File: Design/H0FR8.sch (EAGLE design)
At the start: 43 parts, among them Q1 MMBT3904LT1, U1 STM32G0B1CEU6QFN_B1CEU6_STM-L, U2 T2035H-6GD2PAK_T2550_STM-M, U3 VOT8121AM-VT, U4 TLP184_GR-TPL,SE, U5 V275LA4P, X1 XTALL_CSTCE8M00G52

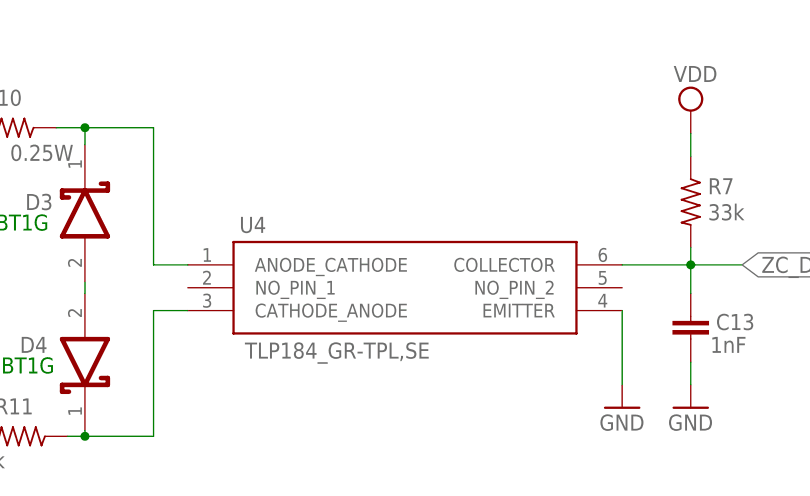
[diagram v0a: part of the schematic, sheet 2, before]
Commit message: - Fixed component's footprints and 3d packages.
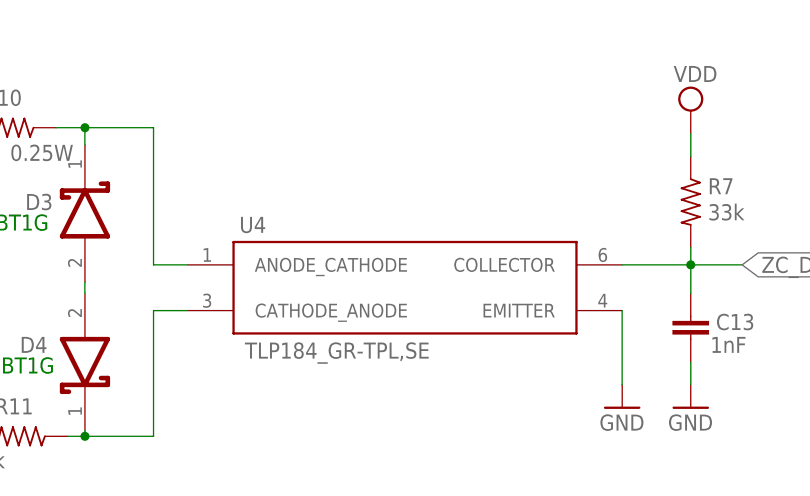
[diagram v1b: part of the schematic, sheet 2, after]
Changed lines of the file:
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@@
 <part name="FB1" library="HEXABITZ_RCLS" library_urn="urn:adsk.eagle:library:20064561" deviceset="FB-0603" device="" package3d_urn="urn:adsk.eagle:package:19666458/5"/>
 <part name="SUPPLY10" library="supply2" library_urn="urn:adsk.eagle:library:372" deviceset="VDD" device=""/>
-<part name="SWD" library="pinhead" deviceset="PINHD-1X3" device="" package3d_urn="urn:adsk.eagle:package:22458/2"/>
+<part name="SWD" library="pinhead" library_urn="urn:adsk.eagle:library:325" deviceset="PINHD-1X3" device="" package3d_urn="urn:adsk.eagle:package:22458/2"/>
 <part name="U1" library="HEXABITZ_ICs" library_urn="urn:adsk.eagle:library:20064554" deviceset="STM32G0B1CEU6" device="QFN_B1CEU6_STM-L" package3d_urn="urn:adsk.eagle:package:33547754/8"/>
 <part name="TRIMBLE-LOGO1" library="HEXABITZ_USER_INTERFACE_PARTS" library_urn="urn:adsk.eagle:library:20064563" deviceset="HEXA-LOGO-SCH" device=""/>
-<part name="TRIMBLE-LOGO2" library="HEXABITZ_USER_INTERFACE_PARTS" library_urn="urn:adsk.eagle:library:20064563" deviceset="HEXA-LOGO" device="" package3d_urn="urn:adsk.eagle:package:43807249/2"/>
+<part name="TRIMBLE-LOGO2" library="HEXABITZ_USER_INTERFACE_PARTS" library_urn="urn:adsk.eagle:library:20064563" deviceset="HEXA-LOGO" device="" package3d_urn="urn:adsk.eagle:package:43807249/3"/>
 <part name="D2" library="HEXABITZ_RCLS" library_urn="urn:adsk.eagle:library:20064561" deviceset="BOURNS_CDSOD323-T03SC" device="BOURNS_CDSOD323-T03SC_0_0" package3d_urn="urn:adsk.eagle:package:20526306/2"/>
 <part name="C10" library="HEXABITZ_RCLS" library_urn="urn:adsk.eagle:library:20064561" deviceset="C-0805" device="" package3d_urn="urn:adsk.eagle:package:19666489/4" value="10nF">
@@
 <part name="R4" library="HEXABITZ_RCLS" library_urn="urn:adsk.eagle:library:20064561" deviceset="R-0603" device="" package3d_urn="urn:adsk.eagle:package:1435818/6" value="1k"/>
 <part name="U2" library="HEXABITZ_ICs" library_urn="urn:adsk.eagle:library:20064554" deviceset="T2035H-6G" device="D2PAK_T2550_STM-M" package3d_urn="urn:adsk.eagle:package:44160048/2"/>
-<part name="U4" library="HEXABITZ_ICs" library_urn="urn:adsk.eagle:library:20064554" deviceset="TLP184_GR-TPL,SE" device="" package3d_urn="urn:adsk.eagle:package:44160045/2"/>
+<part name="U4" library="HEXABITZ_ICs" library_urn="urn:adsk.eagle:library:20064554" deviceset="TLP184_GR-TPL,SE" device="" package3d_urn="urn:adsk.eagle:package:45805681/2"/>
 <part name="U3" library="HEXABITZ_ICs" library_urn="urn:adsk.eagle:library:20064554" deviceset="VOT8121AM-VT" device="" package3d_urn="urn:adsk.eagle:package:44160046/2"/>
-<part name="R12" library="HEXABITZ_RCLS" library_urn="urn:adsk.eagle:library:20064561" deviceset="R-0805" device="" package3d_urn="urn:adsk.eagle:package:19666457/3" value="100">
+<part name="R12" library="HEXABITZ_RCLS" library_urn="urn:adsk.eagle:library:20064561" deviceset="R-0805" device="" package3d_urn="urn:adsk.eagle:package:19666457/4" value="100">
 <attribute name="MPN" value="ERJ-P06J101V"/>
 <attribute name="POWER" value="0.5W"/>
@@
 <attribute name="VOLTAGE_RATING" value="35V"/>
 </part>
-<part name="R6" library="HEXABITZ_RCLS" library_urn="urn:adsk.eagle:library:20064561" deviceset="R-0805" device="" package3d_urn="urn:adsk.eagle:package:19666457/3" value="390">
+<part name="R6" library="HEXABITZ_RCLS" library_urn="urn:adsk.eagle:library:20064561" deviceset="R-0805" device="" package3d_urn="urn:adsk.eagle:package:19666457/4" value="390">
 <attribute name="MPN" value="ERJ-P06J391V"/>
 <attribute name="POWER" value="0.5W"/>
@@
 <attribute name="VOLTAGE_RATING" value="400V"/>
 </part>
-<part name="R13" library="HEXABITZ_RCLS" library_urn="urn:adsk.eagle:library:20064561" deviceset="R-0805" device="" package3d_urn="urn:adsk.eagle:package:19666457/3" value="1.5k">
+<part name="R13" library="HEXABITZ_RCLS" library_urn="urn:adsk.eagle:library:20064561" deviceset="R-0805" device="" package3d_urn="urn:adsk.eagle:package:19666457/4" value="1.5k">
 <attribute name="MPN" value="ERJ-P06J152V"/>
 <attribute name="POWER" value="0.5W"/>
 </part>
-<part name="Q1" library="HEXABITZ_RCLS" library_urn="urn:adsk.eagle:library:20064561" deviceset="MMBT3904LT1" device="" package3d_urn="urn:adsk.eagle:package:19666472/4">
+<part name="Q1" library="HEXABITZ_RCLS" library_urn="urn:adsk.eagle:library:20064561" deviceset="MMBT3904LT1" device="" package3d_urn="urn:adsk.eagle:package:19666472/5">
 <attribute name="MFN" value="ON Semiconductor"/>
 <attribute name="MPN" value="MMBT3904LT1G"/>
@@
 <part name="C13" library="HEXABITZ_RCLS" library_urn="urn:adsk.eagle:library:20064561" deviceset="C-0603" device="" package3d_urn="urn:adsk.eagle:package:19666468/3" value="1nF"/>
 <part name="GND7" library="supply1" library_urn="urn:adsk.eagle:library:371" deviceset="GND" device=""/>
-<part name="D3" library="HEXABITZ_RCLS" library_urn="urn:adsk.eagle:library:20064561" deviceset="STMICROELECTRONICS_BAT46ZFILM" device="STMICROELECTRONICS_BAT46ZFILM_0_3" package3d_urn="urn:adsk.eagle:package:27595196/2"/>
-<part name="D4" library="HEXABITZ_RCLS" library_urn="urn:adsk.eagle:library:20064561" deviceset="STMICROELECTRONICS_BAT46ZFILM" device="STMICROELECTRONICS_BAT46ZFILM_0_3" package3d_urn="urn:adsk.eagle:package:27595196/2"/>
-<part name="R10" library="HEXABITZ_RCLS" library_urn="urn:adsk.eagle:library:20064561" deviceset="R-0805" device="" package3d_urn="urn:adsk.eagle:package:19666457/3" value="100k">
+<part name="D3" library="HEXABITZ_RCLS" library_urn="urn:adsk.eagle:library:20064561" deviceset="STMICROELECTRONICS_BAT46ZFILM" device="STMICROELECTRONICS_BAT46ZFILM_0_3" package3d_urn="urn:adsk.eagle:package:27595196/3"/>
+<part name="D4" library="HEXABITZ_RCLS" library_urn="urn:adsk.eagle:library:20064561" deviceset="STMICROELECTRONICS_BAT46ZFILM" device="STMICROELECTRONICS_BAT46ZFILM_0_3" package3d_urn="urn:adsk.eagle:package:27595196/3"/>
+<part name="R10" library="HEXABITZ_RCLS" library_urn="urn:adsk.eagle:library:20064561" deviceset="R-0805" device="" package3d_urn="urn:adsk.eagle:package:19666457/4" value="100k">
 <attribute name="MFN" value="Yageo"/>
 <attribute name="MPN" value="RC0603JR-070RL"/>
@@
 <part name="SUPPLY9" library="supply2" library_urn="urn:adsk.eagle:library:372" deviceset="VDD" device=""/>
 <part name="SUPPLY12" library="supply2" library_urn="urn:adsk.eagle:library:372" deviceset="VDD" device=""/>
-<part name="R11" library="HEXABITZ_RCLS" library_urn="urn:adsk.eagle:library:20064561" deviceset="R-0805" device="" package3d_urn="urn:adsk.eagle:package:19666457/3" value="100k">
+<part name="R11" library="HEXABITZ_RCLS" library_urn="urn:adsk.eagle:library:20064561" deviceset="R-0805" device="" package3d_urn="urn:adsk.eagle:package:19666457/4" value="100k">
 <attribute name="MPN" value="ERJ-P06J104V"/>
 </part>
@@
 <attribute name="TOLERANCE" value="±1%"/>
 </part>
-<part name="C3" library="HEXABITZ_RCLS" library_urn="urn:adsk.eagle:library:20064561" deviceset="C-0603-POL" device="" package3d_urn="urn:adsk.eagle:package:19666490/2" value="4.7uF">
+<part name="C3" library="HEXABITZ_RCLS" library_urn="urn:adsk.eagle:library:20064561" deviceset="C-0603-POL" device="" package3d_urn="urn:adsk.eagle:package:19666490/3" value="4.7uF">
 <attribute name="CAPACITANCE" value="4.7uF"/>
 <attribute name="MFN" value="Murata"/>
@@
 <attribute name="VOLTAGE_RATING" value="25V"/>
 </part>
-<part name="C2" library="HEXABITZ_RCLS" library_urn="urn:adsk.eagle:library:20064561" deviceset="C-0603-POL" device="" package3d_urn="urn:adsk.eagle:package:19666490/2" value="1uF">
+<part name="C2" library="HEXABITZ_RCLS" library_urn="urn:adsk.eagle:library:20064561" deviceset="C-0603-POL" device="" package3d_urn="urn:adsk.eagle:package:19666490/3" value="1uF">
 <attribute name="CAPACITANCE" value="1.00uF"/>
 <attribute name="MFN" value="Yageo"/>
@@
 <part name="U$2" library="HEXABITZ_OTHER_PARTS" library_urn="urn:adsk.eagle:library:20064671" deviceset="FK244D2PAK" device="" package3d_urn="urn:adsk.eagle:package:44947487/4"/>
 <part name="X2" library="HEXABITZ_CONNECTION_PARTS" library_urn="urn:adsk.eagle:library:20064553" deviceset="AK300/3" device="" package3d_urn="urn:adsk.eagle:package:44667727/2"/>
-<part name="U5" library="HEXABITZ_RCLS" library_urn="urn:adsk.eagle:library:20064561" deviceset="V275LA4P" device="" package3d_urn="urn:adsk.eagle:package:44670769/1"/>
+<part name="U5" library="HEXABITZ_RCLS" library_urn="urn:adsk.eagle:library:20064561" deviceset="V275LA4P" device="" package3d_urn="urn:adsk.eagle:package:44670769/2"/>
 <part name="SUPPLY3" library="HEXABITZ_CONNECTION_PARTS" library_urn="urn:adsk.eagle:library:20064553" deviceset="VSSA" device=""/>
 <part name="SUPPLY6" library="HEXABITZ_CONNECTION_PARTS" library_urn="urn:adsk.eagle:library:20064553" deviceset="VSSA" device=""/>
@@
 <text x="242.6462" y="6.1722" size="1.9304" layer="100" font="vector">www.hexabitz.com</text>
 <text x="182.4228" y="11.2014" size="1.9304" layer="101" font="vector">AC Dimmer Module</text>
-<text x="43.18" y="194.945" size="1.778" layer="150">VDD=3.3 Volts</text>
+<text x="12.065" y="204.47" size="1.778" layer="150">VDD=3.3 Volts</text>
 <text x="168.825" y="94.82" size="1.778" layer="95">Vref Coupling</text>
 <text x="138.98" y="94.82" size="1.778" layer="95">VDDA Coupling</text>
-<text x="252.095" y="141.605" size="1.778" layer="95">BOOT</text>
+<text x="245.11" y="141.605" size="1.778" layer="95">BOOT</text>
 </plain>
 <instances>

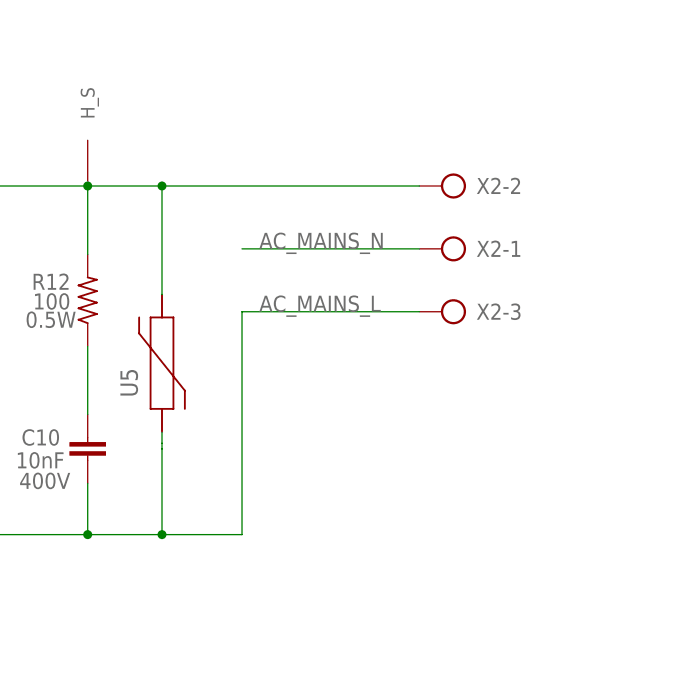
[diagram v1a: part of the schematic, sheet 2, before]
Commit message: - Changed connector. - Fixed nets. - new pcb layout.
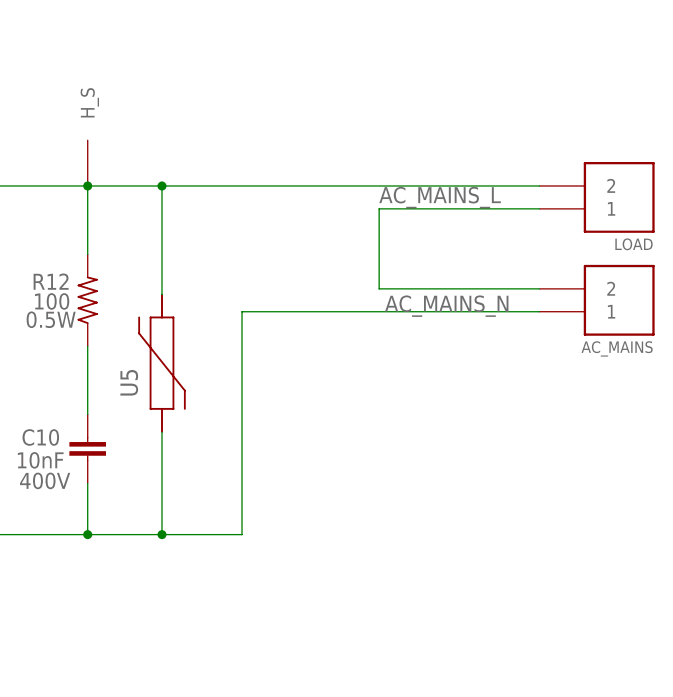
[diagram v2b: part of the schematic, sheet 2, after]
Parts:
- removed X2: (no value), HEXABITZ_CONNECTION_PARTS:AK300/3
- added AC_MAINS, LOAD: (no value), HEXABITZ_CONNECTION_PARTS:1546111-2
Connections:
- net A2: now also LOAD.2; no longer X2-2.KL
- net AC_MAINS_L: now also AC_MAINS.2, LOAD.1; no longer C10.2, C11.2, C9.2, R4.1, U2.A1, U5.1, X2-3.KL
- net AC_MAINS_N: now also AC_MAINS.1, C10.2, C11.2, C9.2, R4.1, U2.A1, U5.1; no longer X2-1.KL
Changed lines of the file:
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@@
 <part name="U$1" library="hexabitz_connectors" library_urn="urn:adsk.eagle:library:20064578" deviceset="HEXABIT_17.32_X3_NO_P1_P2_P3_P4_P5_P6_P11_P12" device="" package3d_urn="urn:adsk.eagle:package:27848120/1"/>
 <part name="U$2" library="HEXABITZ_OTHER_PARTS" library_urn="urn:adsk.eagle:library:20064671" deviceset="FK244D2PAK" device="" package3d_urn="urn:adsk.eagle:package:44947487/4"/>
-<part name="X2" library="HEXABITZ_CONNECTION_PARTS" library_urn="urn:adsk.eagle:library:20064553" deviceset="AK300/3" device="" package3d_urn="urn:adsk.eagle:package:44667727/2"/>
 <part name="U5" library="HEXABITZ_RCLS" library_urn="urn:adsk.eagle:library:20064561" deviceset="V275LA4P" device="" package3d_urn="urn:adsk.eagle:package:44670769/2"/>
 <part name="SUPPLY3" library="HEXABITZ_CONNECTION_PARTS" library_urn="urn:adsk.eagle:library:20064553" deviceset="VSSA" device=""/>
 <part name="SUPPLY6" library="HEXABITZ_CONNECTION_PARTS" library_urn="urn:adsk.eagle:library:20064553" deviceset="VSSA" device=""/>
 <part name="SUPPLY2" library="HEXABITZ_CONNECTION_PARTS" library_urn="urn:adsk.eagle:library:20064553" deviceset="VSSA" device=""/>
+<part name="LOAD" library="HEXABITZ_CONNECTION_PARTS" library_urn="urn:adsk.eagle:library:20064553" deviceset="1546111-2" device="" package3d_urn="urn:adsk.eagle:package:19666461/4"/>
+<part name="AC_MAINS" library="HEXABITZ_CONNECTION_PARTS" library_urn="urn:adsk.eagle:library:20064553" deviceset="1546111-2" device="" package3d_urn="urn:adsk.eagle:package:19666461/4"/>
 </parts>
 <sheets>
@@
 </instance>
 <instance part="U$2" gate="G$1" x="177.165" y="168.91" smashed="yes" rot="R90"/>
-<instance part="X2" gate="-1" x="219.075" y="159.385" smashed="yes" rot="R180">
-<attribute name="NAME" x="220.345" y="158.496" size="1.778" layer="95"/>
-</instance>
-<instance part="X2" gate="-2" x="219.075" y="166.37" smashed="yes" rot="R180">
-<attribute name="NAME" x="220.345" y="165.481" size="1.778" layer="95"/>
-</instance>
-<instance part="X2" gate="-3" x="219.075" y="152.4" smashed="yes" rot="R180">
-<attribute name="NAME" x="220.345" y="151.511" size="1.778" layer="95"/>
-<attribute name="VALUE" x="222.885" y="156.083" size="1.778" layer="96" rot="R180"/>
-</instance>
 <instance part="U5" gate="A" x="185.42" y="133.985" smashed="yes" rot="R90">
 <attribute name="NAME" x="182.7276" y="142.875" size="1.9304" layer="95" ratio="10" rot="SR90"/>
 </instance>
+<instance part="LOAD" gate="G$1" x="237.49" y="166.37" smashed="yes" rot="R180">
+<attribute name="NAME" x="240.03" y="160.528" size="1.27" layer="95" rot="R180"/>
+<attribute name="VALUE" x="240.03" y="170.688" size="1.27" layer="96" rot="R180"/>
+</instance>
+<instance part="AC_MAINS" gate="G$1" x="237.49" y="154.94" smashed="yes" rot="R180">
+<attribute name="NAME" x="240.03" y="149.098" size="1.27" layer="95" rot="R180"/>
+<attribute name="VALUE" x="240.03" y="159.258" size="1.27" layer="96" rot="R180"/>
+</instance>
 </instances>
 <busses>
@@
 </segment>
 <segment>
+<pinref part="AC_MAINS" gate="G$1" pin="2"/>
+<wire x1="227.33" y1="154.94" x2="209.55" y2="154.94" width="0.1524" layer="91"/>
+<label x="209.55" y="164.465" size="1.778" layer="95"/>
+<pinref part="LOAD" gate="G$1" pin="1"/>
+<wire x1="227.33" y1="163.83" x2="209.55" y2="163.83" width="0.1524" layer="91"/>
+<wire x1="209.55" y1="163.83" x2="209.55" y2="154.94" width="0.1524" layer="91"/>
+</segment>
+</net>
+<net name="AC_MAINS_N" class="1">
+<segment>
+<wire x1="83.82" y1="51.435" x2="64.135" y2="51.435" width="0.1524" layer="91"/>
+<label x="64.77" y="51.435" size="1.778" layer="95"/>
+<pinref part="R11" gate="G$1" pin="2"/>
+</segment>
+<segment>
 <pinref part="U2" gate="A" pin="A1"/>
 <wire x1="114.935" y1="168.91" x2="111.125" y2="168.91" width="0.1524" layer="91"/>
@@
 <pinref part="C10" gate="G$1" pin="2"/>
 <wire x1="177.165" y1="127.635" x2="177.165" y2="133.35" width="0.1524" layer="91"/>
-<wire x1="185.42" y1="137.795" x2="185.42" y2="137.16" width="0.1524" layer="91"/>
 <junction x="185.42" y="127.635"/>
 <pinref part="C11" gate="G$1" pin="2"/>
-<wire x1="185.42" y1="137.16" x2="185.42" y2="127.635" width="0.1524" layer="91"/>
+<wire x1="185.42" y1="139.065" x2="185.42" y2="127.635" width="0.1524" layer="91"/>
 <wire x1="164.465" y1="133.35" x2="164.465" y2="127.635" width="0.1524" layer="91"/>
 <junction x="164.465" y="127.635"/>
-<pinref part="X2" gate="-3" pin="KL"/>
-<wire x1="213.995" y1="152.4" x2="194.31" y2="152.4" width="0.1524" layer="91"/>
-<label x="196.215" y="152.4" size="1.778" layer="95"/>
 <pinref part="U5" gate="A" pin="1"/>
-<wire x1="185.42" y1="137.795" x2="185.42" y2="139.065" width="0.1524" layer="91"/>
-</segment>
-</net>
-<net name="AC_MAINS_N" class="1">
-<segment>
-<wire x1="83.82" y1="51.435" x2="64.135" y2="51.435" width="0.1524" layer="91"/>
-<label x="64.77" y="51.435" size="1.778" layer="95"/>
-<pinref part="R11" gate="G$1" pin="2"/>
-</segment>
-<segment>
-<wire x1="213.995" y1="159.385" x2="194.31" y2="159.385" width="0.1524" layer="91"/>
-<pinref part="X2" gate="-1" pin="KL"/>
-<label x="196.215" y="159.385" size="1.778" layer="95"/>
+<pinref part="AC_MAINS" gate="G$1" pin="1"/>
+<wire x1="194.31" y1="152.4" x2="227.33" y2="152.4" width="0.1524" layer="91"/>
+<label x="210.185" y="152.4" size="1.778" layer="95"/>
 </segment>
 </net>
@@
 <junction x="164.465" y="166.37"/>
 <pinref part="U$2" gate="G$1" pin="H_S"/>
-<pinref part="X2" gate="-2" pin="KL"/>
-<wire x1="185.42" y1="166.37" x2="213.995" y2="166.37" width="0.1524" layer="91"/>
-<junction x="185.42" y="166.37"/>
 <pinref part="U5" gate="A" pin="2"/>
+<pinref part="LOAD" gate="G$1" pin="2"/>
+<wire x1="227.33" y1="166.37" x2="185.42" y2="166.37" width="0.1524" layer="91"/>
+<junction x="185.42" y="166.37"/>
 </segment>
 </net>
